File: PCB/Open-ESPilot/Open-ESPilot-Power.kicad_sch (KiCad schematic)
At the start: 1 part, among them U2 AMS1117-3.3

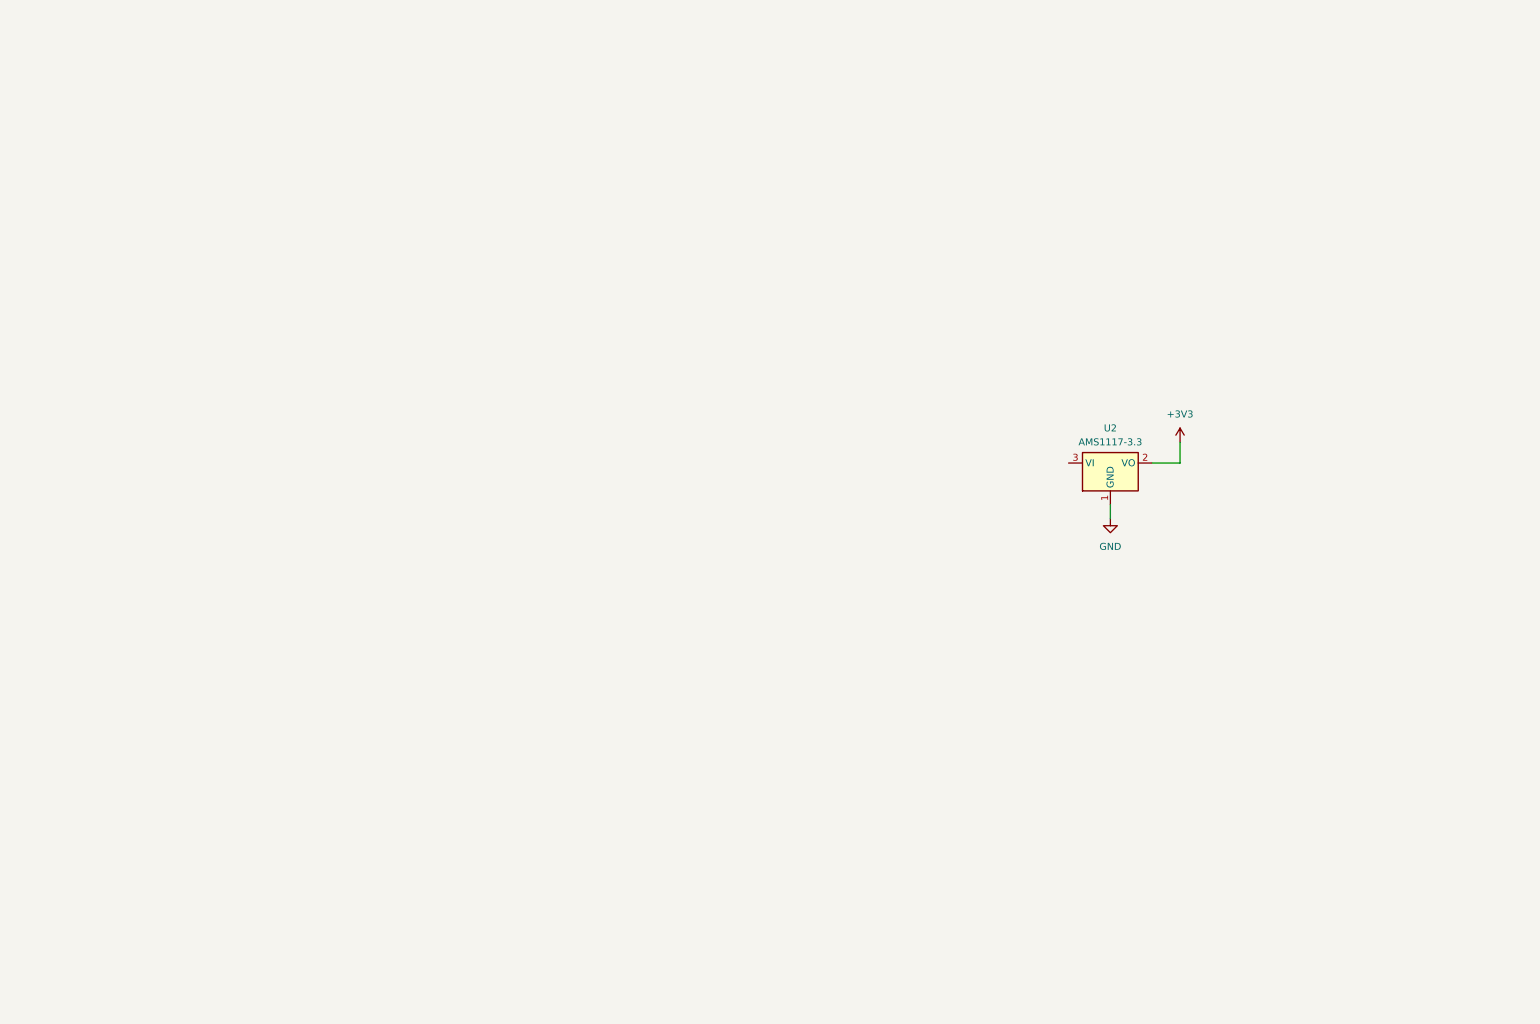
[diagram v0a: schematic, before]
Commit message: Worked on the Power Schematic. Added voltage input and a switching regulator. Fixed the LDO.
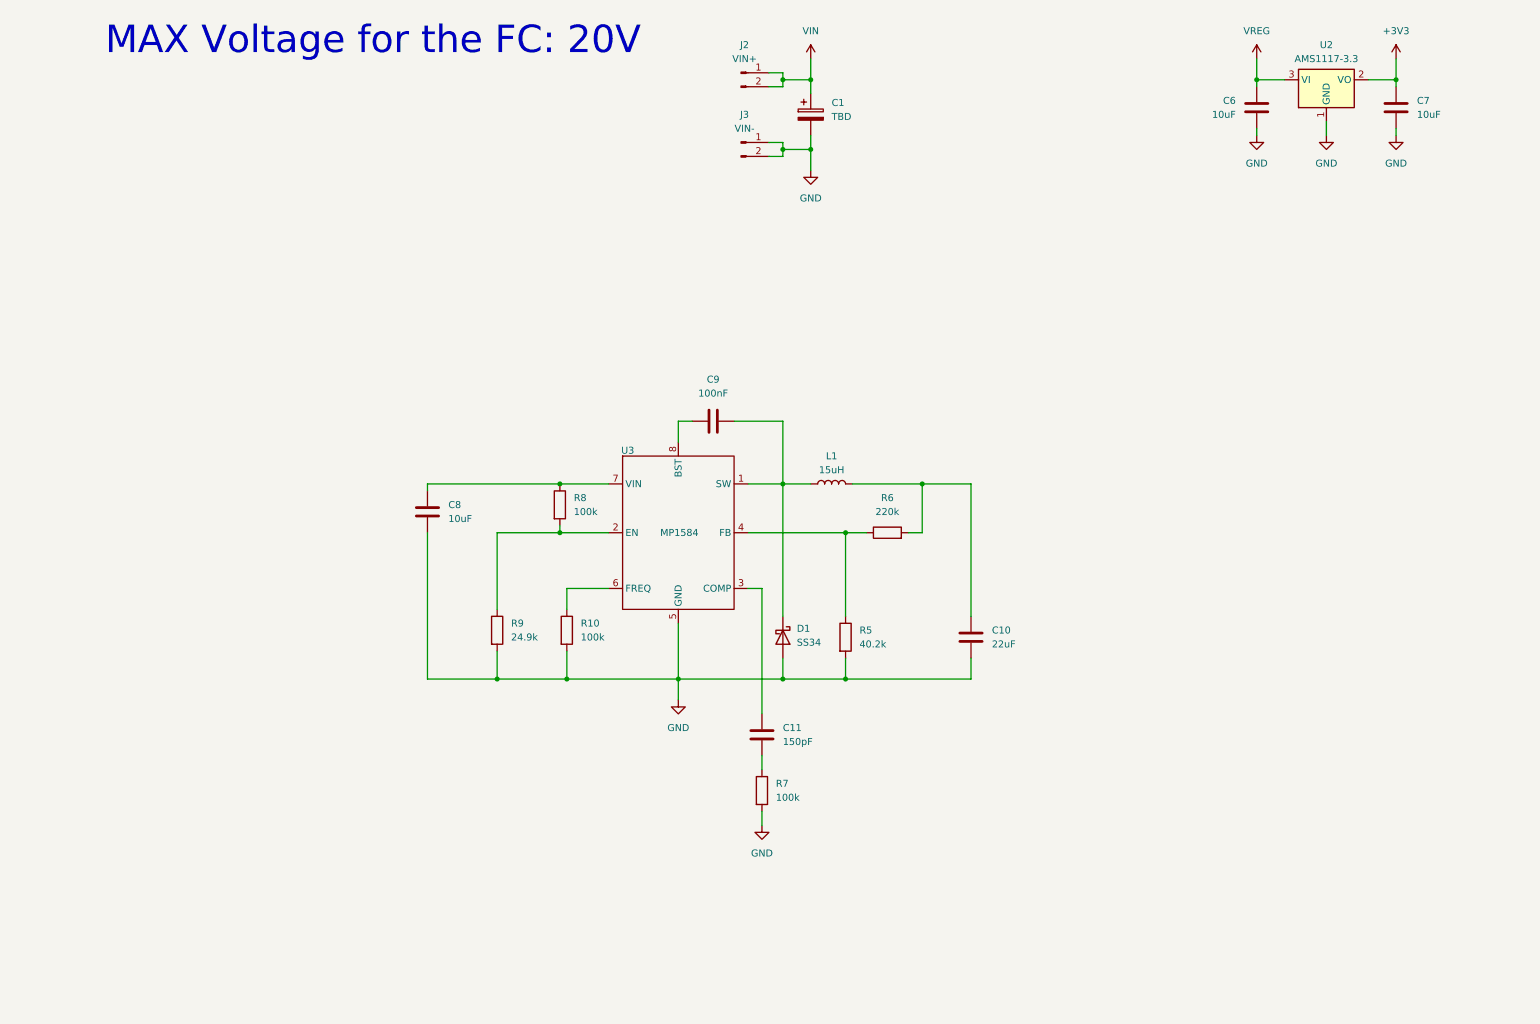
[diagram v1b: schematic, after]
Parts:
- added C1: TBD, symbol Device:C_Polarized
- added C10: 22uF, symbol Device:C
- added C11: 150pF, symbol Device:C
- added C6, C7, C8: 10uF, symbol Device:C
- added C9: 100nF, symbol Device:C
- added D1: SS34, symbol Device:D_Schottky
- added J2: VIN+, symbol Connector:Conn_01x02_Pin
- added J3: VIN-, symbol Connector:Conn_01x02_Pin
- added L1: 15uH, symbol Device:L
- added R10, R7, R8: 100k, symbol Device:R
- added R5: 40.2k, symbol Device:R
- added R6: 220k, symbol Device:R
- added R9: 24.9k, symbol Device:R
- added U3: MP1584, Package_SO:SOIC-8_3.9x4.9mm_P1.27mm, symbol MP1584:MP1584
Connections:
- net +3V3: now also C7.1
- net GND: now also C1.2, C10.2, C6.2, C7.2, C8.2, D1.2 (A), J3.1 (Pin_1), J3.2 (Pin_2), R10.2, R5.2, R7.2, R9.2, U3.5 (GND)
- net VREG: now reaches U2.3 (VI)
- net VREG: now also C6.1
- new net: R5.1, R6.1, U3.4 (FB)
- new net: C10.1, L1.2, R6.2
- new net: C11.2, R7.1
- new net: C8.1, R8.1, U3.7 (VIN)
- new net: C11.1, U3.3 (COMP)
- new net: R8.2, R9.1, U3.2 (EN)
- new net: C9.2, D1.1 (K), L1.1, U3.1 (SW)
- new net: R10.1, U3.6 (FREQ)
- new net: C9.1, U3.8 (BST)
- new net VIN: C1.1, J2.1 (Pin_1), J2.2 (Pin_2)
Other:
- note added: "MAX Voltage for the FC: 20V"
- moved on the sheet: U2

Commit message: Edited Power schematic and insted of the IC I have decided to use modules.
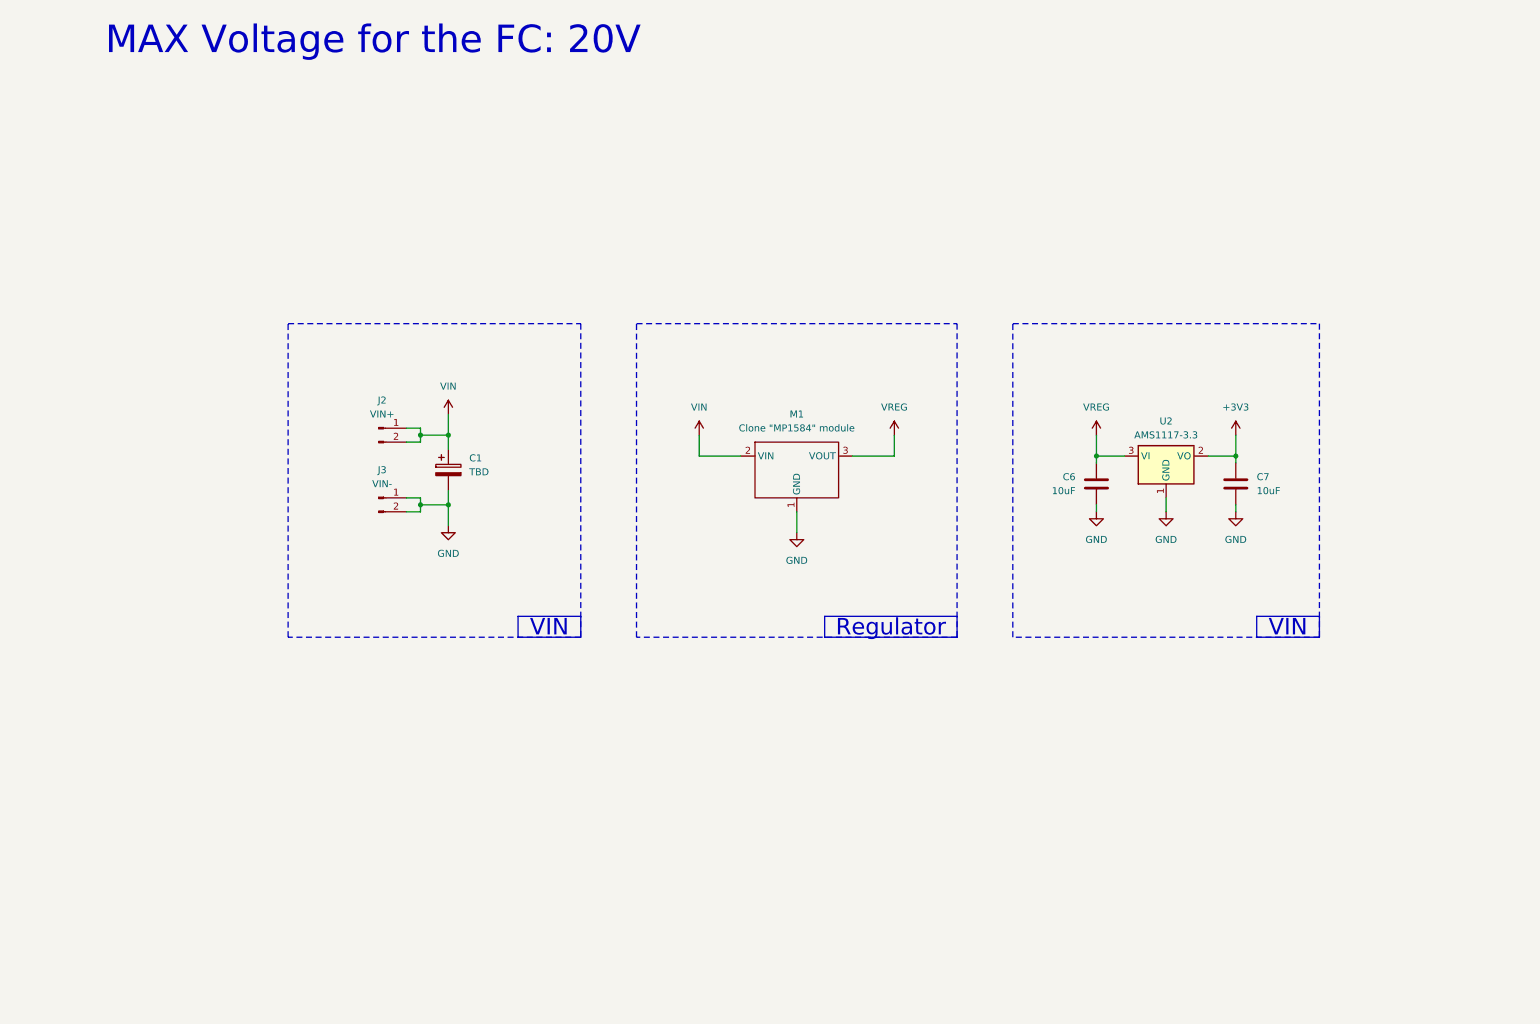
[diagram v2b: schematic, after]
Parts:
- removed C10: 22uF, symbol Device:C
- removed C11: 150pF, symbol Device:C
- removed C8: 10uF, symbol Device:C
- removed C9: 100nF, symbol Device:C
- removed D1: SS34, symbol Device:D_Schottky
- removed L1: 15uH, symbol Device:L
- removed R10, R7, R8: 100k, symbol Device:R
- removed R5: 40.2k, symbol Device:R
- removed R6: 220k, symbol Device:R
- removed R9: 24.9k, symbol Device:R
- removed U3: MP1584, Package_SO:SOIC-8_3.9x4.9mm_P1.27mm, symbol MP1584:MP1584
- added M1: Clone "MP1584" module, symbol Clone {dblquote}MP1584{dblquote} module:Clone_{dblquote}MP1584{dblquote}_module
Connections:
- net GND: now also M1.1 (GND)
- net VIN: now also M1.2 (VIN)
- net VREG: now also M1.3 (VOUT)
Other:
- moved on the sheet: C1, C6, C7, J2, J3, U2

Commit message: Edited the MP1584 module and added Schematic and footprint of the GY-91 and implemented it to the schematic.
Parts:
- M1: footprint (none) -> Clone "MP1584" module:Clone _MP1584_ module
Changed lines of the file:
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@@
 			)
 		)
-		(property "Footprint" ""
+		(property "Footprint" "Clone \"MP1584\" module:Clone _MP1584_ module"
 			(at 146.05 96.52 0)
 			(effects

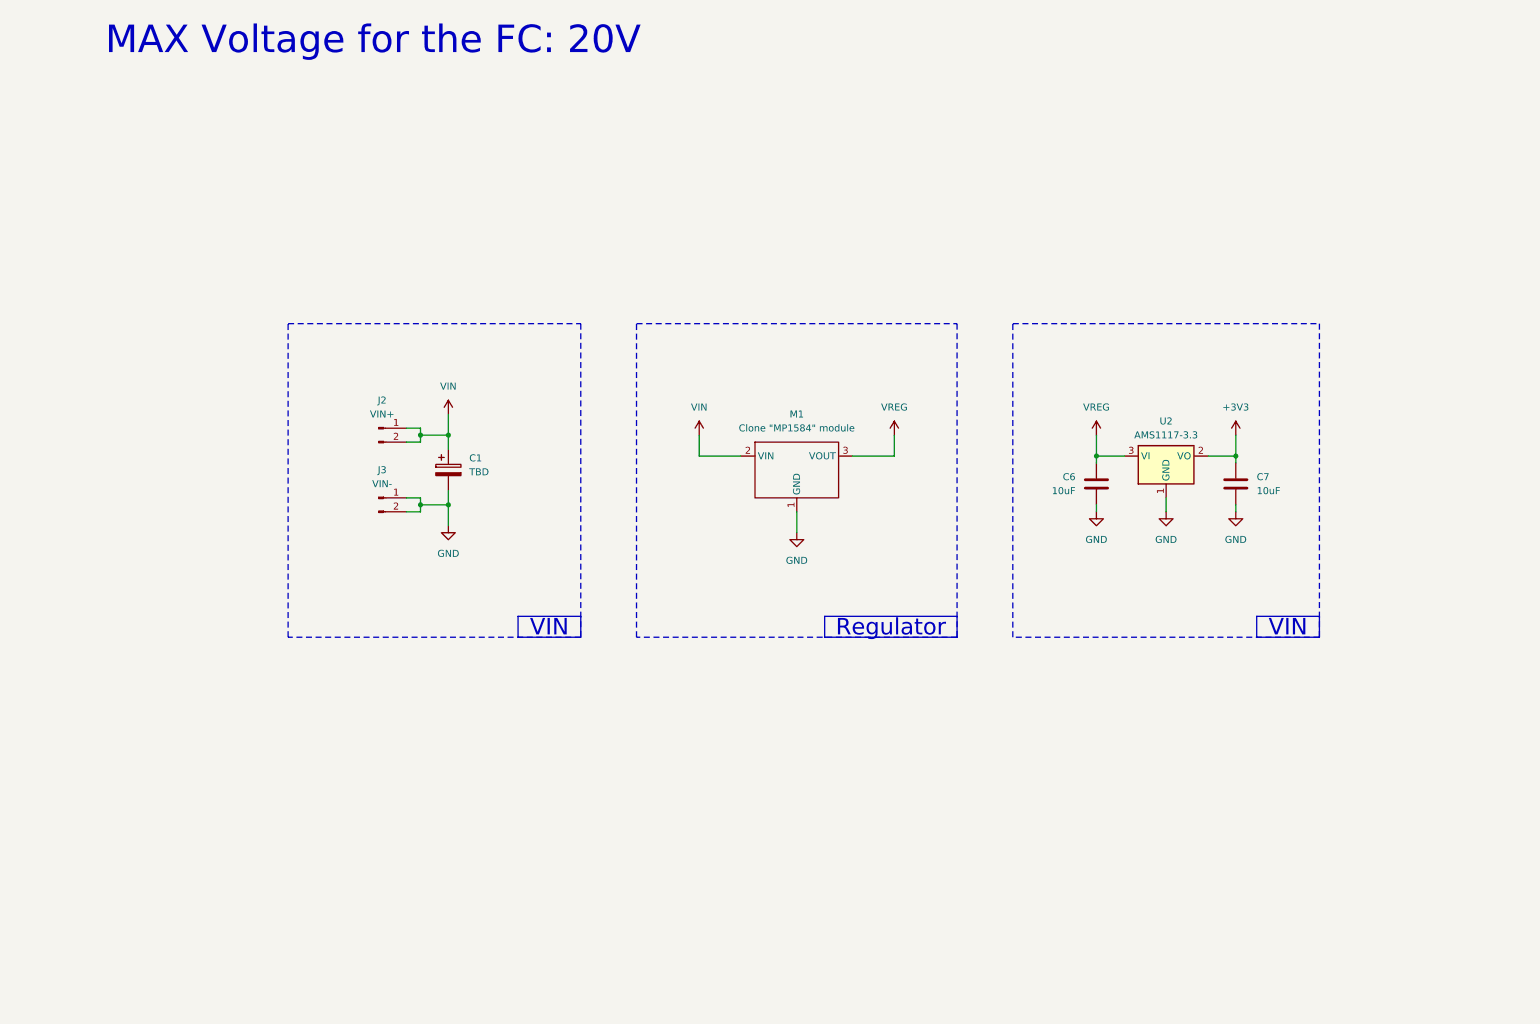
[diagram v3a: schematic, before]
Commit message: Edited Pin definitions to Open ESPilot. And added the pheripherials to the schematic. Also new journal entry.
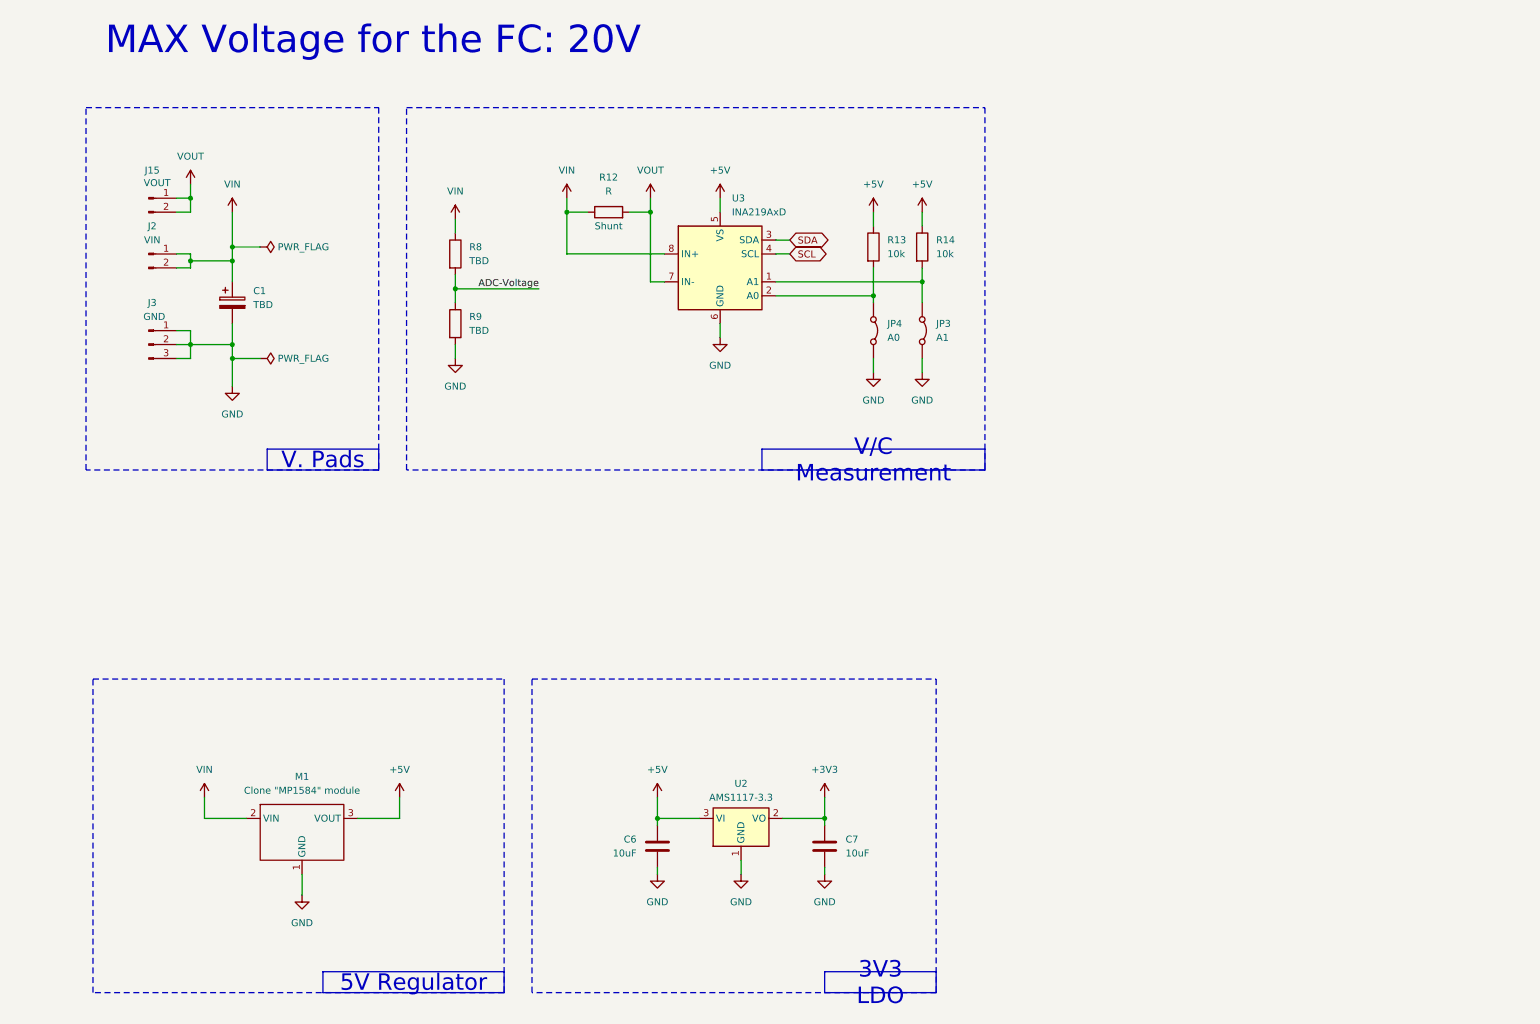
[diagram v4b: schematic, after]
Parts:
- added J15: VOUT, symbol Connector:Conn_01x02_Pin
- added JP3: A1, symbol Jumper:Jumper_2_Bridged
- added JP4: A0, symbol Jumper:Jumper_2_Bridged
- added R12: R, Resistor_THT:R_Axial_Shunt_L35.3mm_W9.5mm_PS25.40mm_P38.10mm, symbol Device:R
- added R13, R14: 10k, symbol Device:R
- added R8, R9: TBD, symbol Device:R
- added U3: INA219AxD, Package_SO:SOIC-8_3.9x4.9mm_P1.27mm, symbol Sensor_Energy:INA219AxD
- J2: value VIN+ -> VIN
- J3: value VIN- -> GND; symbol Connector:Conn_01x02_Pin -> Connector:Conn_01x03_Pin
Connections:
- net GND: now also J3.3 (Pin_3), JP3.2 (B), JP4.2 (B), R9.2, U3.6 (GND)
- net VIN: now also R12.1, R8.1, U3.8 (IN+)
- net VREG renamed +5V
- net +5V: now also R13.1, R14.1, U3.5 (VS)
- new net: JP4.1 (A), R13.2, U3.2 (A0)
- new net: JP3.1 (A), R14.2, U3.1 (A1)
- new net ADC-Voltage: R8.2, R9.1
- new net SCL: U3.4 (SCL)
- new net SDA: U3.3 (SDA)
- new net VOUT: J15.1 (Pin_1), J15.2 (Pin_2), R12.2, U3.7 (IN-)
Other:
- moved on the sheet: C1, C6, C7, J2, M1, U2

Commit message: Schematic Fixes
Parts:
- added C10, C11: 10uF, symbol Device:C
- added C12: 100nF, symbol Device:C
- added C9: TBD, symbol Device:C_Polarized
- added D13: B5819W, Diode_SMD:D_SOD-123, symbol Device:D_Schottky
- added D2, D8: PDZVTR5.1B, Diode_SMD:D_SOD-128, symbol Device:D_Zener
- added D3: SSA34, Diode_SMD:D_SMA, symbol Device:D_Schottky
- added F1: Polyfuse, symbol Device:Polyfuse
- added JP5: REG/USB, symbol Jumper:Jumper_3_Bridged12
- added Q3: AO3401A, Package_TO_SOT_SMD:SOT-23, symbol Transistor_FET:AO3401A
- added R15: 10k, Resistor_SMD:R_0603_1608Metric_Pad0.98x0.95mm_HandSolder, symbol Device:R_Small
- added U8: AMS1117-3.3, Package_TO_SOT_SMD:SOT-89-3, symbol Regulator_Linear:AMS1117-3.3
- C6, C7, U2: now not fitted; now left out of the parts list
- M1: footprint Clone "MP1584" module:Clone _MP1584_ module -> Clone _MP1584_ module:Clone _MP1584_ module; symbol Clone {dblquote}MP1584{dblquote} module:Clone_{dblquote}MP1584{dblquote}_module -> Clone _MP1584_ module:Clone _MP1584_ module
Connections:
- net +3V3: now also C11.1, U8.2 (VO)
- net +5V: now also C10.1, C12.1, C9.1, D13.1 (K), D8.1 (K), JP5.2 (C), Q3.2 (S), U8.3 (VI); no longer M1.3 (VOUT)
- net ADC-Voltage: now also D2.1 (K)
- net GND: now also C10.2, C11.2, C12.2, C9.2, D2.2 (A), D8.2 (A), R15.2, U8.1 (GND)
- net VIN: now also F1.1; no longer M1.2 (VIN)
- new net: D3.1 (K), M1.2 (VIN)
- new net: D3.2 (A), F1.2
- new net +5Vreg: JP5.1 (A), M1.3 (VOUT), Q3.3 (D)
- new net +5Vusb: D13.2 (A), JP5.3 (B), Q3.1 (G), R15.1
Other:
- note added: "Backup selector"
- note added: "Smaller footprint"
- moved on the sheet: C1, J15, J2, J3, JP3, JP4, M1, R12, R13, R14, R8, R9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
